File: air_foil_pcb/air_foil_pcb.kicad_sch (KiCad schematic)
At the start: 4 parts, among them J1 Raspberry_Pi_2_3, U1 TCA9548APWR

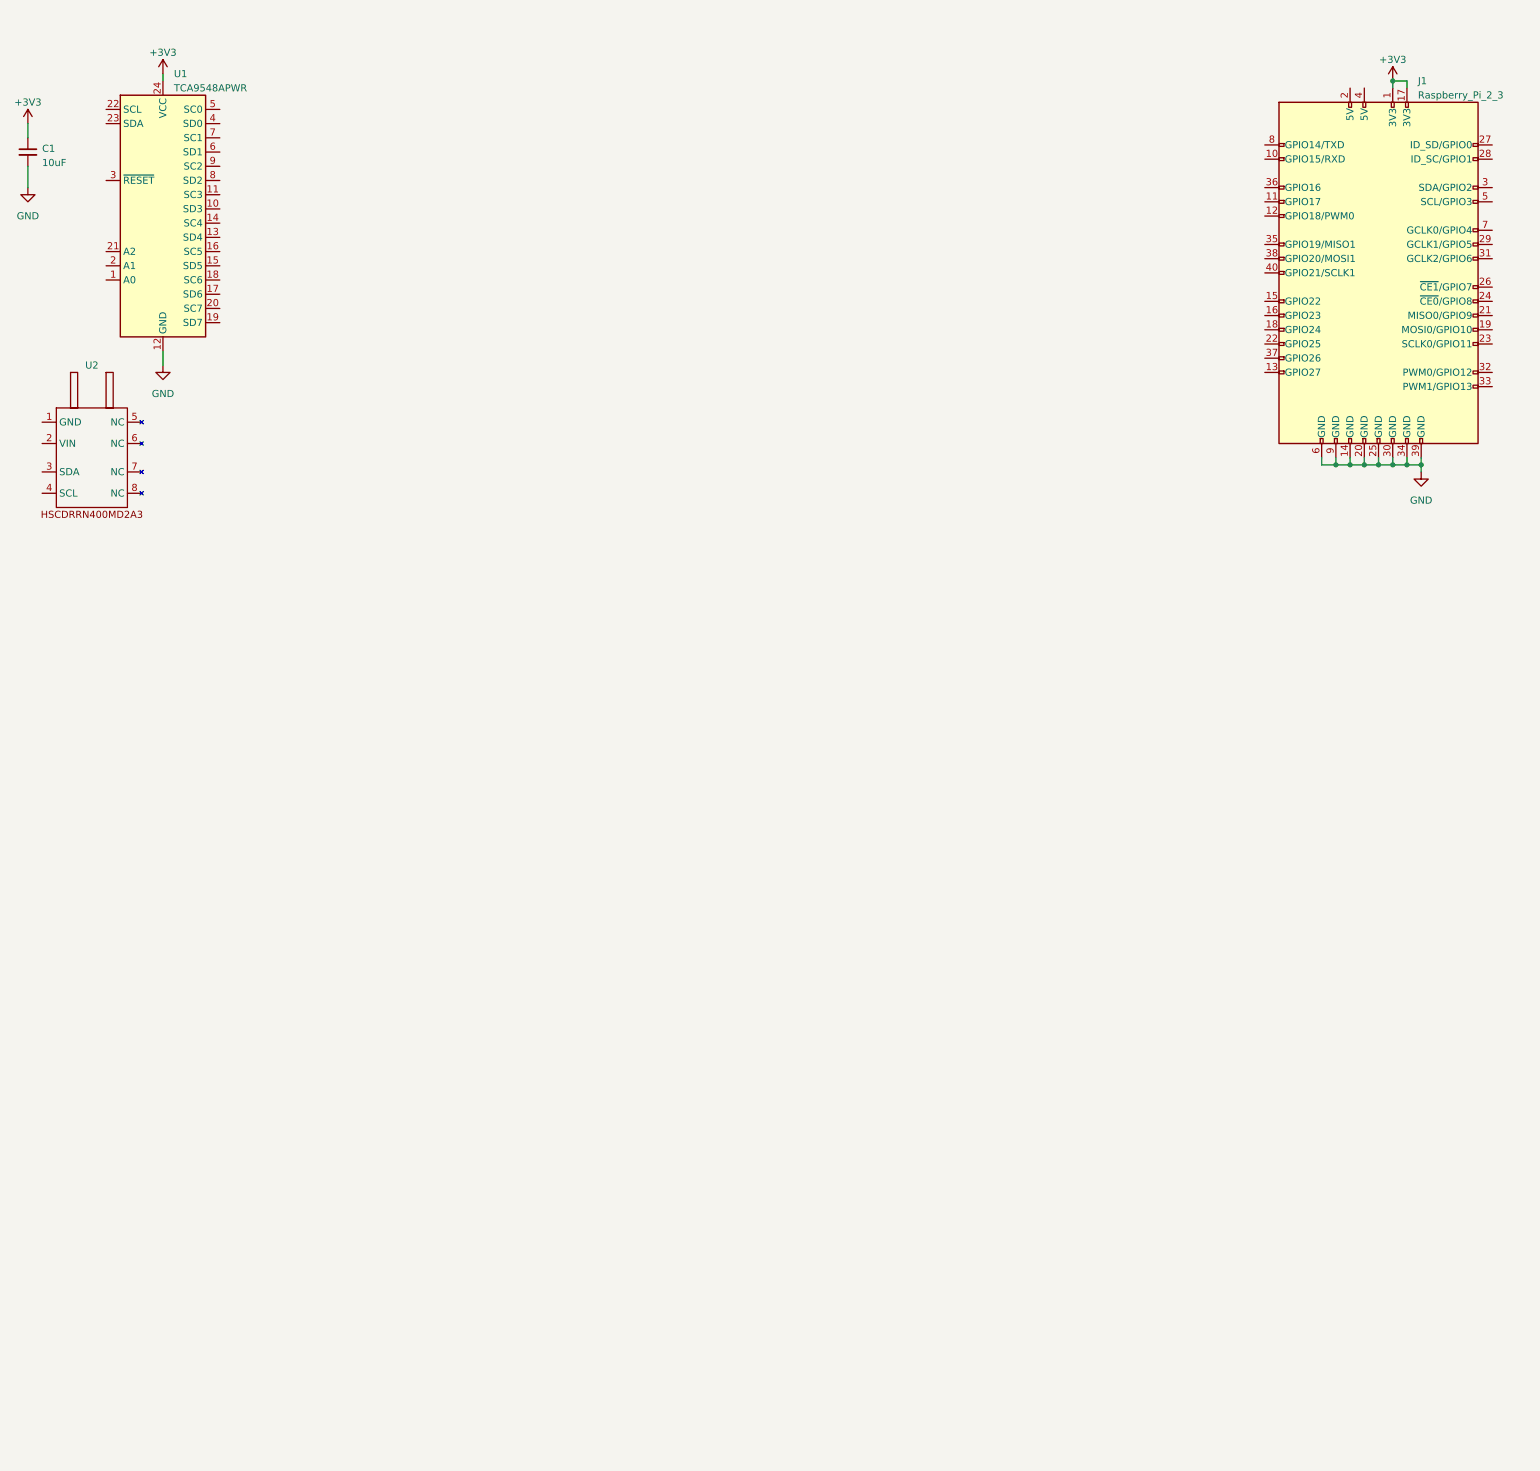
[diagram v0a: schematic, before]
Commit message: made adjustment to pressure sensor schematic, schematic for first multiplexer and associated sensor completed
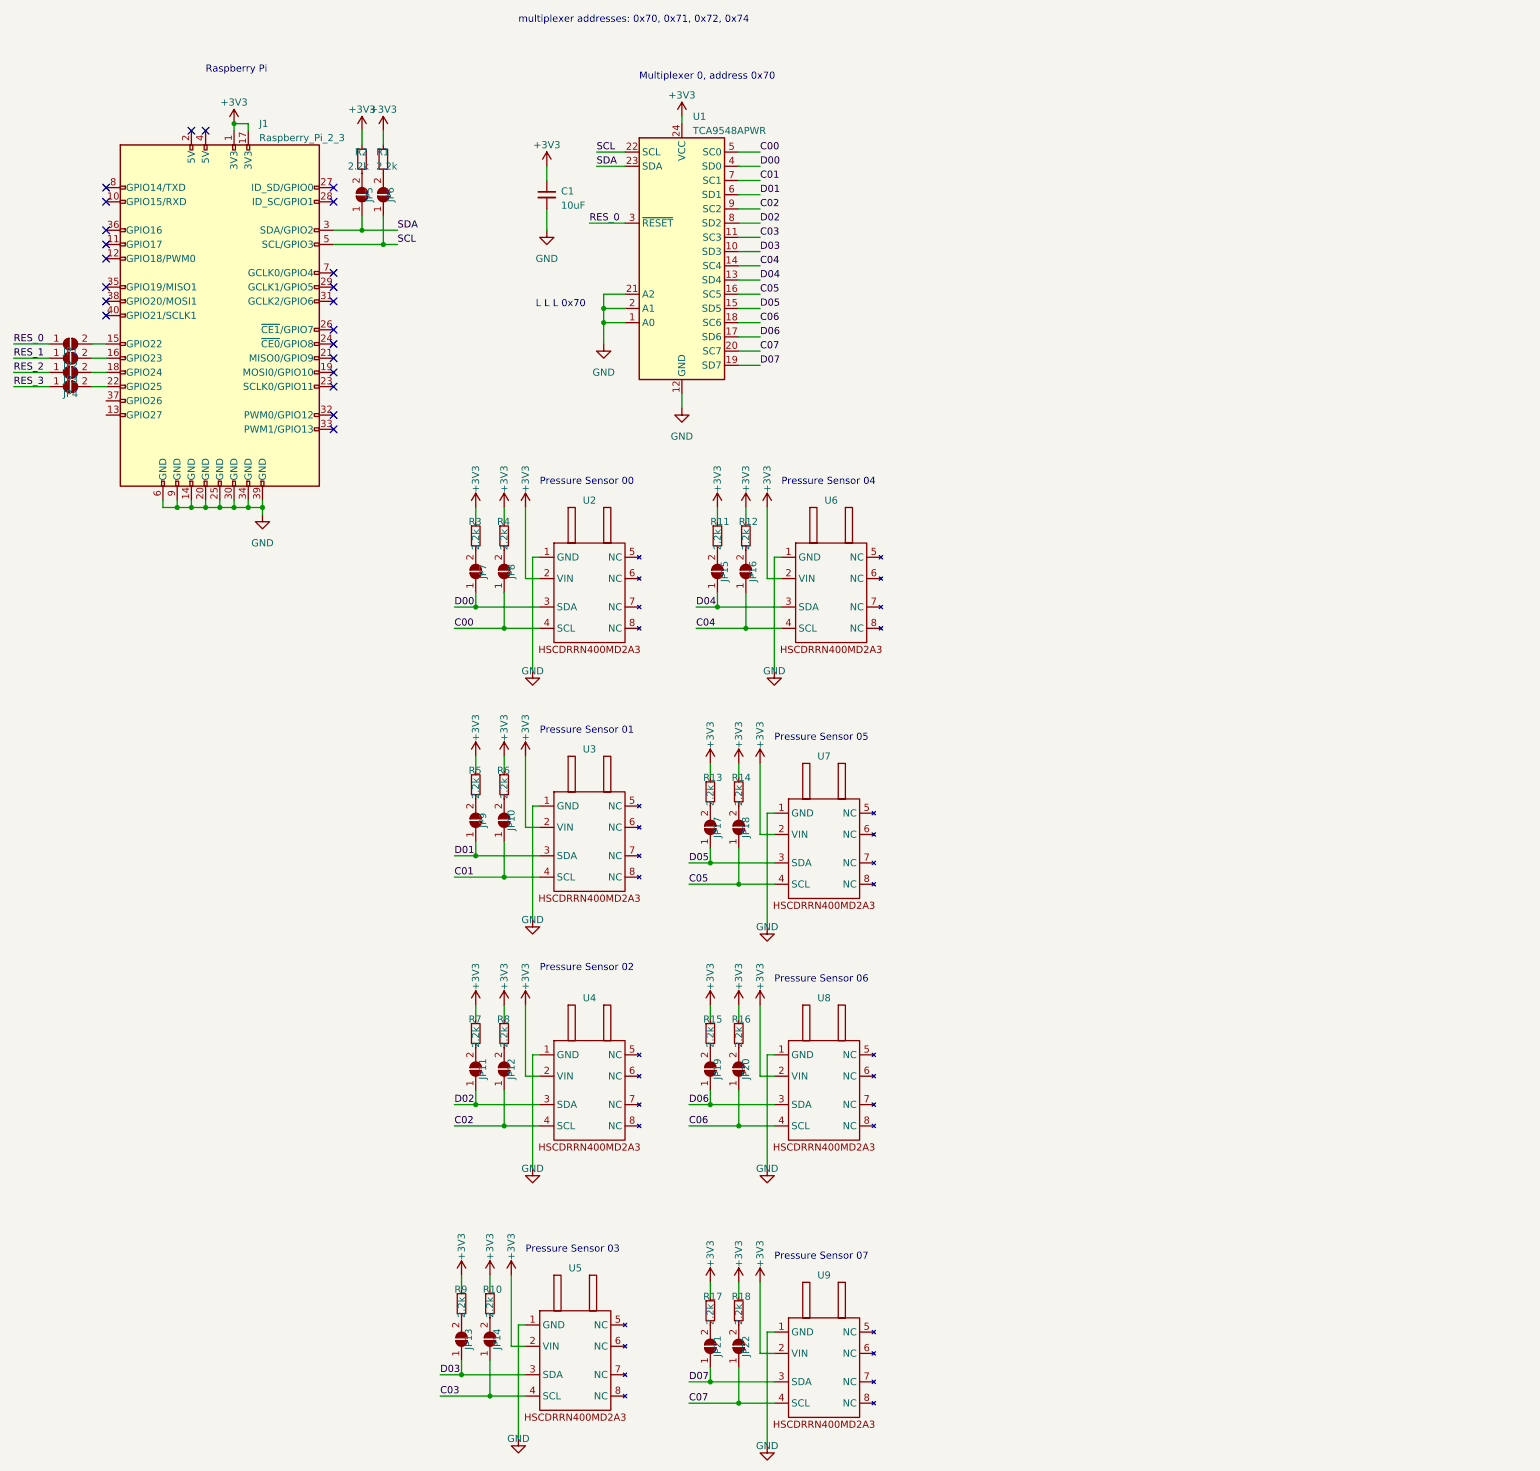
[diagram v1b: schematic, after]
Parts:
- added JP1, JP10, JP11, JP12, JP13, JP14, JP15, JP16, JP17, JP18, JP19, JP2, JP20, JP21, JP22, JP3, JP4, JP5, JP6, JP7, JP8, JP9: SolderJumper_2_Open, symbol Jumper:SolderJumper_2_Open
- added R1, R10, R11, R12, R13, R14, R15, R16, R17, R18, R2, R3, R4, R5, R6, R7, R8, R9: 2.2k, symbol Device:R_Small
- added U3, U4, U5, U6, U7, U8, U9: ~, symbol air_foil_symbols:HSCDRRN400MD2A3
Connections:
- net +3V3: now also U2.2 (VIN), R1.1, R10.1, R11.1, R12.1, R13.1, R14.1, R15.1, R16.1, R17.1, R18.1, R2.1, R3.1, R4.1, R5.1, R6.1, R7.1, R8.1, R9.1, U3.2 (VIN), U4.2 (VIN), U5.2 (VIN), U6.2 (VIN), U7.2 (VIN), U8.2 (VIN), U9.2 (VIN)
- net GND: now also U1.1 (A0), U1.2 (A1), U1.21 (A2), U2.1 (GND), U3.1 (GND), U4.1 (GND), U5.1 (GND), U6.1 (GND), U7.1 (GND), U8.1 (GND), U9.1 (GND)
- net at J1.15 (GPIO22): now also JP1.2 (B)
- net at J1.16 (GPIO23): now also JP2.2 (B)
- net at J1.18 (GPIO24): now also JP3.2 (B)
- net at J1.22 (GPIO25): now also JP4.2 (B)
- net SDA: now reaches J1.3 (SDA/GPIO2)
- net SDA: now also U1.23 (SDA), JP5.1 (A)
- net SCL: now reaches J1.5 (SCL/GPIO3)
- net SCL: now also U1.22 (SCL), JP6.1 (A)
- net D03: now reaches U1.10 (SD3)
- net D03: now also JP13.1 (A), U5.3 (SDA)
- net C03: now reaches U1.11 (SC3)
- net C03: now also JP14.1 (A), U5.4 (SCL)
- net D04: now reaches U1.13 (SD4)
- net D04: now also JP15.1 (A), U6.3 (SDA)
- net C04: now reaches U1.14 (SC4)
- net C04: now also JP16.1 (A), U6.4 (SCL)
- net D05: now reaches U1.15 (SD5)
- net D05: now also JP17.1 (A), U7.3 (SDA)
- net C05: now reaches U1.16 (SC5)
- net C05: now also JP18.1 (A), U7.4 (SCL)
- net D06: now reaches U1.17 (SD6)
- net D06: now also JP19.1 (A), U8.3 (SDA)
- net C06: now reaches U1.18 (SC6)
- net C06: now also JP20.1 (A), U8.4 (SCL)
- net D07: now reaches U1.19 (SD7)
- net D07: now also JP21.1 (A), U9.3 (SDA)
- net C07: now reaches U1.20 (SC7)
- net C07: now also JP22.1 (A), U9.4 (SCL)
- net RES_0: now reaches U1.3 (~{RESET})
- net RES_0: now also JP1.1 (A)
- net D00: now reaches U1.4 (SD0)
- net D00: now also U2.3 (SDA), JP7.1 (A)
- net C00: now reaches U1.5 (SC0)
- net C00: now also U2.4 (SCL), JP8.1 (A)
- net D01: now reaches U1.6 (SD1)
- net D01: now also JP9.1 (A), U3.3 (SDA)
- net C01: now reaches U1.7 (SC1)
- net C01: now also JP10.1 (A), U3.4 (SCL)
- net D02: now reaches U1.8 (SD2)
- net D02: now also JP11.1 (A), U4.3 (SDA)
- net C02: now reaches U1.9 (SC2)
- net C02: now also JP12.1 (A), U4.4 (SCL)
- new net: JP21.2 (B), R17.2
- new net: JP16.2 (B), R12.2
- new net: JP5.2 (B), R2.2
- new net: JP17.2 (B), R13.2
- new net: JP10.2 (B), R6.2
- new net: JP12.2 (B), R8.2
- new net: JP18.2 (B), R14.2
- new net: JP8.2 (B), R4.2
- new net: JP19.2 (B), R15.2
- new net: JP14.2 (B), R10.2
- new net: JP15.2 (B), R11.2
- new net: JP22.2 (B), R18.2
- new net: JP11.2 (B), R7.2
- new net: JP9.2 (B), R5.2
- new net: JP13.2 (B), R9.2
- new net: JP7.2 (B), R3.2
- new net: JP20.2 (B), R16.2
- new net: JP6.2 (B), R1.2
- new net RES_1: JP2.1 (A)
- new net RES_2: JP3.1 (A)
- new net RES_3: JP4.1 (A)
- no-connect marks 0 -> 22
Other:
- note added: "L L L 0x70"
- note added: "Multiplexer 0, address 0x70"
- note added: "Pressure Sensor 00"
- note added: "Pressure Sensor 01"
- note added: "Pressure Sensor 02"
- note added: "Pressure Sensor 03"
- note added: "Pressure Sensor 04"
- note added: "Pressure Sensor 05"
- note added: "Pressure Sensor 06"
- note added: "Pressure Sensor 07"
- note added: "Raspberry Pi"
- note added: "multiplexer addresses: 0x70, 0x71, 0x72, 0x74"
- moved on the sheet: C1, J1, U1, U2

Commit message: finished schematic, added tube connector
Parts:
- added C10, C11, C12, C13, C14, C15, C16, C17, C18, C19, C2, C20, C21, C22, C23, C24, C25, C26, C27, C28, C29, C3, C30, C31, C32, C33, C34, C35, C36, C4, C5, C6, C7, C8, C9: 10uF, symbol Device:C_Small
- added J2: ~, symbol air_foil_symbols:TubeConnector
- added JP23, JP24, JP25, JP26, JP27, JP28, JP29, JP30, JP31, JP32, JP33, JP34, JP35, JP36, JP37, JP38, JP39, JP40, JP41, JP42, JP43, JP44, JP45, JP46, JP47, JP48, JP49, JP50, JP51, JP52, JP53, JP54, JP55, JP56, JP57, JP58, JP59, JP60, JP61, JP62, JP63, JP64, JP65, JP66, JP67, JP68, JP69, JP70: SolderJumper_2_Open, symbol Jumper:SolderJumper_2_Open
- added R19, R20, R21, R22, R23, R24, R25, R26, R27, R28, R29, R30, R31, R32, R33, R34, R35, R36, R37, R38, R39, R40, R41, R42, R43, R44, R45, R46, R47, R48, R49, R50, R51, R52, R53, R54, R55, R56, R57, R58, R59, R60, R61, R62, R63, R64, R65, R66: 2.2k, symbol Device:R_Small
- added U10, U11, U12, U13, U15, U16, U17, U18, U19, U20, U21, U22, U24, U25, U26, U27, U28, U29, U30, U31, U33, U34, U35, U36: ~, symbol air_foil_symbols:HSCDRRN400MD2A3
- added U14, U23, U32: TCA9548APWR, Package_SO:TSSOP-24_4.4x7.8mm_P0.65mm, symbol Interface_Expansion:TCA9548APWR
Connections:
- net +3V3: now also C10.1, C11.1, C12.1, C13.1, C14.1, C15.1, C16.1, C17.1, C18.1, C19.1, C2.1, C20.1, C21.1, C22.1, C23.1, C24.1, C25.1, C26.1, C27.1, C28.1, C29.1, C3.1, C30.1, C31.1, C32.1, C33.1, C34.1, C35.1, C36.1, C4.1, C5.1, C6.1, C7.1, C8.1, C9.1, R19.1, R20.1, R21.1, R22.1, R23.1, R24.1, R25.1, R26.1, R27.1, R28.1, R29.1, R30.1, R31.1, R32.1, R33.1, R34.1, R35.1, R36.1, R37.1, R38.1, R39.1, R40.1, R41.1, R42.1, R43.1, R44.1, R45.1, R46.1, R47.1, R48.1, R49.1, R50.1, R51.1, R52.1, R53.1, R54.1, R55.1, R56.1, R57.1, R58.1, R59.1, R60.1, R61.1, R62.1, R63.1, R64.1, R65.1, R66.1, U10.2 (VIN), U11.2 (VIN), U12.2 (VIN), U13.2 (VIN), U14.1 (A0), U14.24 (VCC), U15.2 (VIN), U16.2 (VIN), U17.2 (VIN), U18.2 (VIN), U19.2 (VIN), U20.2 (VIN), U21.2 (VIN), U22.2 (VIN), U23.2 (A1), U23.24 (VCC), U24.2 (VIN), U25.2 (VIN), U26.2 (VIN), U27.2 (VIN), U28.2 (VIN), U29.2 (VIN), U30.2 (VIN), U31.2 (VIN), U32.21 (A2), U32.24 (VCC), U33.2 (VIN), U34.2 (VIN), U35.2 (VIN), U36.2 (VIN)
- net GND: now also C10.2, C11.2, C12.2, C13.2, C14.2, C15.2, C16.2, C17.2, C18.2, C19.2, C2.2, C20.2, C21.2, C22.2, C23.2, C24.2, C25.2, C26.2, C27.2, C28.2, C29.2, C3.2, C30.2, C31.2, C32.2, C33.2, C34.2, C35.2, C36.2, C4.2, C5.2, C6.2, C7.2, C8.2, C9.2, U10.1 (GND), U11.1 (GND), U12.1 (GND), U13.1 (GND), U14.12 (GND), U14.2 (A1), U14.21 (A2), U15.1 (GND), U16.1 (GND), U17.1 (GND), U18.1 (GND), U19.1 (GND), U20.1 (GND), U21.1 (GND), U22.1 (GND), U23.1 (A0), U23.12 (GND), U23.21 (A2), U24.1 (GND), U25.1 (GND), U26.1 (GND), U27.1 (GND), U28.1 (GND), U29.1 (GND), U30.1 (GND), U31.1 (GND), U32.1 (A0), U32.12 (GND), U32.2 (A1), U33.1 (GND), U34.1 (GND), U35.1 (GND), U36.1 (GND)
- net RES_1: now also U14.3 (~{RESET})
- net RES_2: now also U23.3 (~{RESET})
- net RES_3: now also U32.3 (~{RESET})
- net SCL: now also U14.22 (SCL), U23.22 (SCL), U32.22 (SCL)
- net SDA: now also U14.23 (SDA), U23.23 (SDA), U32.23 (SDA)
- new net: JP42.2 (B), R38.2
- new net: JP66.2 (B), R62.2
- new net: JP55.2 (B), R51.2
- new net: JP59.2 (B), R55.2
- new net: JP34.2 (B), R30.2
- new net: JP35.2 (B), R31.2
- new net: JP63.2 (B), R59.2
- new net: JP32.2 (B), R28.2
- new net: JP23.2 (B), R19.2
- new net: JP56.2 (B), R52.2
- new net: JP28.2 (B), R24.2
- new net: JP29.2 (B), R25.2
- new net: JP40.2 (B), R36.2
- new net: JP64.2 (B), R60.2
- new net: JP68.2 (B), R64.2
- new net: JP62.2 (B), R58.2
- new net: JP41.2 (B), R37.2
- new net: JP43.2 (B), R39.2
- new net: JP67.2 (B), R63.2
- new net: JP45.2 (B), R41.2
- new net: JP39.2 (B), R35.2
- new net: JP53.2 (B), R49.2
- new net: JP54.2 (B), R50.2
- new net: JP46.2 (B), R42.2
- new net: JP57.2 (B), R53.2
- new net: JP50.2 (B), R46.2
- new net: JP27.2 (B), R23.2
- new net: JP61.2 (B), R57.2
- new net: JP38.2 (B), R34.2
- new net: JP51.2 (B), R47.2
- new net: JP36.2 (B), R32.2
- new net: JP44.2 (B), R40.2
- new net: JP60.2 (B), R56.2
- new net: JP49.2 (B), R45.2
- new net: JP48.2 (B), R44.2
- new net: JP37.2 (B), R33.2
- new net: JP58.2 (B), R54.2
- new net: JP33.2 (B), R29.2
- new net: JP31.2 (B), R27.2
- new net: JP70.2 (B), R66.2
- new net: JP65.2 (B), R61.2
- new net: JP26.2 (B), R22.2
- new net: JP24.2 (B), R20.2
- new net: JP25.2 (B), R21.2
- new net: JP69.2 (B), R65.2
- new net: JP52.2 (B), R48.2
- new net: JP47.2 (B), R43.2
- new net: JP30.2 (B), R26.2
- new net C10: JP28.1 (A), U11.4 (SCL), U14.5 (SC0)
- new net C11: JP29.1 (A), U12.4 (SCL), U14.7 (SC1)
- new net C12: JP30.1 (A), U13.4 (SCL), U14.9 (SC2)
- new net C13: JP27.1 (A), U10.4 (SCL), U14.11 (SC3)
- new net C14: JP38.1 (A), U14.14 (SC4), U18.4 (SCL)
- new net C15: JP35.1 (A), U14.16 (SC5), U15.4 (SCL)
- new net C16: JP36.1 (A), U14.18 (SC6), U16.4 (SCL)
- new net C17: JP37.1 (A), U14.20 (SC7), U17.4 (SCL)
- new net C20: JP44.1 (A), U20.4 (SCL), U23.5 (SC0)
- new net C21: JP45.1 (A), U21.4 (SCL), U23.7 (SC1)
- new net C22: JP46.1 (A), U22.4 (SCL), U23.9 (SC2)
- new net C23: JP43.1 (A), U19.4 (SCL), U23.11 (SC3)
- new net C24: JP54.1 (A), U23.14 (SC4), U27.4 (SCL)
- new net C25: JP51.1 (A), U23.16 (SC5), U24.4 (SCL)
- new net C26: JP52.1 (A), U23.18 (SC6), U25.4 (SCL)
- new net C27: JP53.1 (A), U23.20 (SC7), U26.4 (SCL)
- new net C30: JP60.1 (A), U29.4 (SCL), U32.5 (SC0)
- new net C31: JP61.1 (A), U30.4 (SCL), U32.7 (SC1)
- new net C32: JP62.1 (A), U31.4 (SCL), U32.9 (SC2)
- new net C33: JP59.1 (A), U28.4 (SCL), U32.11 (SC3)
- new net C34: JP70.1 (A), U32.14 (SC4), U36.4 (SCL)
- new net C35: JP67.1 (A), U32.16 (SC5), U33.4 (SCL)
- new net C36: JP68.1 (A), U32.18 (SC6), U34.4 (SCL)
- new net C37: JP69.1 (A), U32.20 (SC7), U35.4 (SCL)
- new net D10: JP24.1 (A), U11.3 (SDA), U14.4 (SD0)
- new net D11: JP25.1 (A), U12.3 (SDA), U14.6 (SD1)
- new net D12: JP26.1 (A), U13.3 (SDA), U14.8 (SD2)
- new net D13: JP23.1 (A), U10.3 (SDA), U14.10 (SD3)
- new net D14: JP34.1 (A), U14.13 (SD4), U18.3 (SDA)
- new net D15: JP31.1 (A), U14.15 (SD5), U15.3 (SDA)
- new net D16: JP32.1 (A), U14.17 (SD6), U16.3 (SDA)
- new net D17: JP33.1 (A), U14.19 (SD7), U17.3 (SDA)
- new net D20: JP40.1 (A), U20.3 (SDA), U23.4 (SD0)
- new net D21: JP41.1 (A), U21.3 (SDA), U23.6 (SD1)
- new net D22: JP42.1 (A), U22.3 (SDA), U23.8 (SD2)
- new net D23: JP39.1 (A), U19.3 (SDA), U23.10 (SD3)
- new net D24: JP50.1 (A), U23.13 (SD4), U27.3 (SDA)
- new net D25: JP47.1 (A), U23.15 (SD5), U24.3 (SDA)
- new net D26: JP48.1 (A), U23.17 (SD6), U25.3 (SDA)
- new net D27: JP49.1 (A), U23.19 (SD7), U26.3 (SDA)
- new net D30: JP56.1 (A), U29.3 (SDA), U32.4 (SD0)
- new net D31: JP57.1 (A), U30.3 (SDA), U32.6 (SD1)
- new net D32: JP58.1 (A), U31.3 (SDA), U32.8 (SD2)
- new net D33: JP55.1 (A), U28.3 (SDA), U32.10 (SD3)
- new net D34: JP66.1 (A), U32.13 (SD4), U36.3 (SDA)
- new net D35: JP63.1 (A), U32.15 (SD5), U33.3 (SDA)
- new net D36: JP64.1 (A), U32.17 (SD6), U34.3 (SDA)
- new net D37: JP65.1 (A), U32.19 (SD7), U35.3 (SDA)
- no-connect marks 22 -> 24
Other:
- note added: "Filtering capacitors for power inputs to pressure sensors"
- note added: "H L L 0x74"
- note added: "L H L 0x72"
- note added: "L L H 0x71"
- note added: "Multiplexer 1, address 0x71"
- note added: "Multiplexer 2, address 0x72"
- note added: "Multiplexer 3, address 0x74"
- note added: "Pressure Sensor 10"
- note added: "Pressure Sensor 11"
- note added: "Pressure Sensor 12"
- note added: "Pressure Sensor 13"
- note added: "Pressure Sensor 14"
- note added: "Pressure Sensor 15"
- note added: "Pressure Sensor 16"
- note added: "Pressure Sensor 17"
- note added: "Pressure Sensor 20"
- note added: "Pressure Sensor 21"
- note added: "Pressure Sensor 22"
- note added: "Pressure Sensor 23"
- note added: "Pressure Sensor 24"
- note added: "Pressure Sensor 25"
- note added: "Pressure Sensor 26"
- note added: "Pressure Sensor 27"
- note added: "Pressure Sensor 30"
- note added: "Pressure Sensor 31"
- note added: "Pressure Sensor 32"
- note added: "Pressure Sensor 33"
- note added: "Pressure Sensor 34"
- note added: "Pressure Sensor 35"
- note added: "Pressure Sensor 36"
- note added: "Pressure Sensor 37"
- note added: "Tube connector"
- moved on the sheet: C1, JP10, JP11, JP12, JP13, JP14, JP15, JP16, JP17, JP18, JP19, JP20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

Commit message: added 0.1uF caps to power inputs for high frequency filtering
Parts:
- added C37, C38, C39, C40, C41, C42, C43, C44, C45, C46, C47, C48, C49, C50, C51, C52, C53, C54, C55, C56, C57, C58, C59, C60, C61, C62, C63, C64, C65, C66, C67, C68, C69, C70, C71, C72: 0.1uF, symbol Device:C_Small
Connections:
- net +3V3: now also C37.1, C38.1, C39.1, C40.1, C41.1, C42.1, C43.1, C44.1, C45.1, C46.1, C47.1, C48.1, C49.1, C50.1, C51.1, C52.1, C53.1, C54.1, C55.1, C56.1, C57.1, C58.1, C59.1, C60.1, C61.1, C62.1, C63.1, C64.1, C65.1, C66.1, C67.1, C68.1, C69.1, C70.1, C71.1, C72.1
- net GND: now also C37.2, C38.2, C39.2, C40.2, C41.2, C42.2, C43.2, C44.2, C45.2, C46.2, C47.2, C48.2, C49.2, C50.2, C51.2, C52.2, C53.2, C54.2, C55.2, C56.2, C57.2, C58.2, C59.2, C60.2, C61.2, C62.2, C63.2, C64.2, C65.2, C66.2, C67.2, C68.2, C69.2, C70.2, C71.2, C72.2
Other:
- moved on the sheet: C1, C2, C3, JP10, JP11, JP12, JP13, JP14, JP15, JP16, JP17, JP18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

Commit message: working on schematic
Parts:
- removed JP1, JP2, JP3, JP4: SolderJumper_2_Open, symbol Jumper:SolderJumper_2_Open
- added J3: Brass Manifold, air_foil_pcb:static_pressure_manifold, symbol air_foil_symbols:brass_manifold
- added J4: End_plate_mount, air_foil_pcb:end_plate_connector, symbol air_foil_symbols:End_plate_mount
- added J5: Conn_01x10, Connector_PinHeader_2.54mm:PinHeader_1x10_P2.54mm_Horizontal, symbol Connector_Generic:Conn_01x10
- C1, C10, C11, C12, C13, C14, C15, C16, C17, C18, C19, C2, C20, C21, C22, C23, C24, C25, C26, C27, C28, C29, C3, C30, C31, C32, C33, C34, C35, C36, C4, C5, C6, C7, C8, C9: footprint (none) -> Capacitor_SMD:C_0201_0603Metric; JLCPCB_Part_num (none) -> C96446; notes (none) -> 0603
- C37, C38, C39, C40, C41, C42, C43, C44, C45, C46, C47, C48, C49, C50, C51, C52, C53, C54, C55, C56, C57, C58, C59, C60, C61, C62, C63, C64, C65, C66, C67, C68, C69, C70, C71, C72: footprint (none) -> Capacitor_SMD:C_0201_0603Metric; JLCPCB_Part_num (none) -> C14663; notes (none) -> 0603 footprint
- J2: value ~ -> Tube Connector; footprint (none) -> air_foil_pcb:tube_connector
- JP10, JP11, JP12, JP13, JP14, JP15, JP16, JP17, JP18, JP19, JP20, JP21, JP22, JP23, JP24, JP25, JP26, JP27, JP28, JP29, JP30, JP31, JP32, JP33, JP34, JP35, JP36, JP37, JP38, JP39, JP40, JP41, JP42, JP43, JP44, JP45, JP46, JP47, JP48, JP49, JP5, JP50, JP51, JP52, JP53, JP54, JP55, JP56, JP57, JP58, JP59, JP6, JP60, JP61, JP62, JP63, JP64, JP65, JP66, JP67, JP68, JP69, JP7, JP70, JP8, JP9: footprint (none) -> Jumper:SolderJumper-2_P1.3mm_Open_TrianglePad1.0x1.5mm
- R1, R10, R11, R12, R13, R14, R15, R16, R17, R18, R19, R2, R20, R21, R22, R23, R24, R25, R26, R27, R28, R29, R3, R30, R31, R32, R33, R34, R35, R36, R37, R38, R39, R4, R40, R41, R42, R43, R44, R45, R46, R47, R48, R49, R5, R50, R51, R52, R53, R54, R55, R56, R57, R58, R59, R6, R60, R61, R62, R63, R64, R65, R66, R7, R8, R9: footprint (none) -> Resistor_SMD:R_01005_0402Metric; JLCPCB_Part_num (none) -> C25879; notes (none) -> 0402
- U1, U14, U23, U32: JLCPCB_Part_num (none) -> C130026
- U10, U11, U12, U13, U15, U16, U17, U18, U19, U2, U20, U21, U22, U24, U25, U26, U27, U28, U29, U3, U30, U31, U33, U34, U35, U36, U4, U5, U6, U7, U8, U9: value ~ -> HSCDRRN400MD2A3; footprint (none) -> air_foil_pcb:hscdrrn400md2a3
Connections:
- net +3V3: now also J5.1 (Pin_1), J5.2 (Pin_2)
- net GND: now also J5.10 (Pin_10), J5.9 (Pin_9)
- net RES_0: now also J1.15 (GPIO22), J5.6 (Pin_6)
- net RES_1: now also J1.16 (GPIO23), J5.5 (Pin_5)
- net RES_2: now also J1.18 (GPIO24), J5.4 (Pin_4)
- net RES_3: now also J1.22 (GPIO25), J5.3 (Pin_3)
- net SCL: now also J5.8 (Pin_8)
- net SDA: now also J5.7 (Pin_7)
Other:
- note added: "Brass Manifold"

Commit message: fab files created
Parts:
- C1, C10, C11, C12, C13, C14, C15, C16, C17, C18, C19, C2, C20, C21, C22, C23, C24, C25, C26, C27, C28, C29, C3, C30, C31, C32, C33, C34, C35, C36, C4, C5, C6, C7, C8, C9: LCSC (none) -> C96446
- C37, C38, C39, C40, C41, C42, C43, C44, C45, C46, C47, C48, C49, C50, C51, C52, C53, C54, C55, C56, C57, C58, C59, C60, C61, C62, C63, C64, C65, C66, C67, C68, C69, C70, C71, C72: LCSC (none) -> C14663
- J5: LCSC (none) -> C86750
- R1, R10, R11, R12, R13, R14, R15, R16, R17, R18, R19, R2, R20, R21, R22, R23, R24, R25, R26, R27, R28, R29, R3, R30, R31, R32, R33, R34, R35, R36, R37, R38, R39, R4, R40, R41, R42, R43, R44, R45, R46, R47, R48, R49, R5, R50, R51, R52, R53, R54, R55, R56, R57, R58, R59, R6, R60, R61, R62, R63, R64, R65, R66, R7, R8, R9: LCSC (none) -> C25879
- U1, U14, U23, U32: LCSC (none) -> C130026
